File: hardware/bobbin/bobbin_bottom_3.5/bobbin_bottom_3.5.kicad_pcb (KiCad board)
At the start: 2 copper layers, 78.5 x 8.5 mm, 5 parts, among them J1 OC, J2 OC, J3 IC, J4 IC

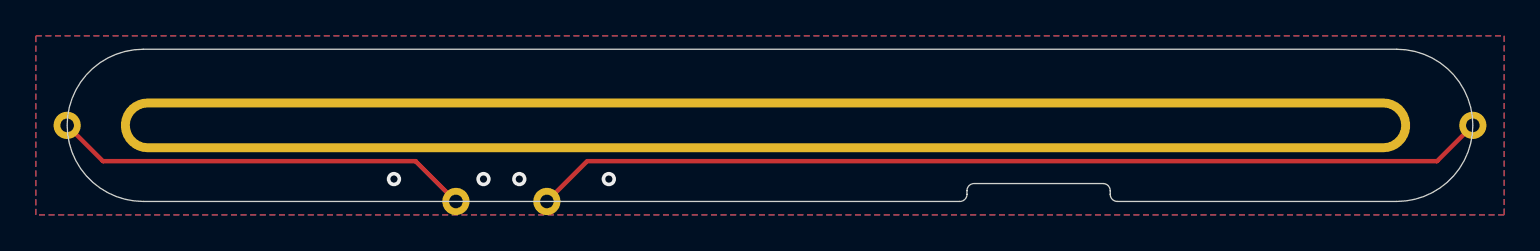
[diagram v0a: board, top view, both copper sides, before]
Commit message: adjusted for proper mouse-bites in panels
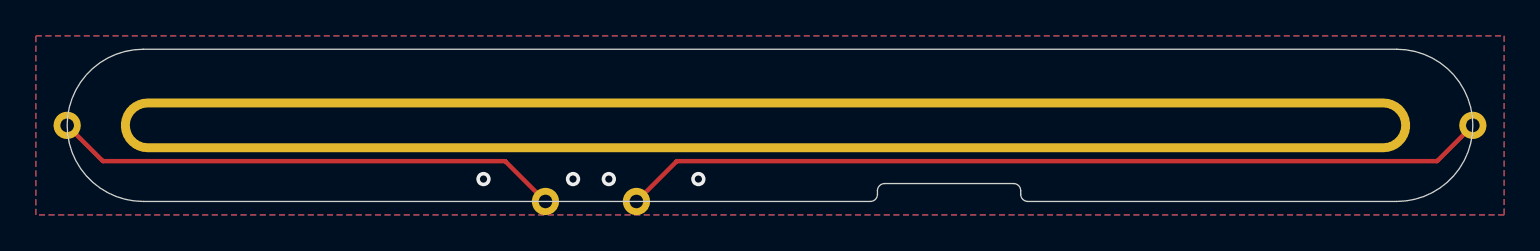
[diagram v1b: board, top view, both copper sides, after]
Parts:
- moved J1 5.00 mm to (122.5, 105.2)
- moved J4 5.00 mm to (117.5, 105.2)
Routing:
- net /OC: track 53.5 -> 48.5 mm
- net /IC: track 23.5 -> 28.5 mm
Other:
- outline, holes or cut-outs redrawn
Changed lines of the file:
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@@
   (net 3 "/IC")
   (footprint "cycfi_library:single-pad-1.52x1.52-th" (layer "F.Cu")
-    (at 117.54 105.25 180)
+    (at 122.54 105.25 180)
     (property "Sheetfile" "bobbin_bottom_3.5.kicad_sch")
     (property "Sheetname" "")
     (attr through_hole)
-    (fp_text reference "J1" (at 0 2.54 180) (layer "F.SilkS") hide
+    (fp_text reference "J1" (at 0 2.54) (layer "F.SilkS") hide
       (effects (font (size 1 1) (thickness 0.15)))
     )
-    (fp_text value "OC" (at 0 -2.54 180) (layer "F.Fab")
+    (fp_text value "OC" (at 0 -2.54) (layer "F.Fab")
       (effects (font (size 1 1) (thickness 0.15)))
     )
@@
   )
   (footprint "cycfi_library:single-pad-1.52x1.52-th" (layer "F.Cu")
-    (at 112.46 105.25)
+    (at 117.46 105.25)
     (property "Sheetfile" "bobbin_bottom_3.5.kicad_sch")
     (property "Sheetname" "")
@@
   (gr_line (start 95 100) (end 95 102) (layer "Dwgs.User") (width 0.01))
   (gr_arc (start 95 105.25) (mid 90.75 101) (end 95 96.75) (layer "Dwgs.User") (width 0.01))
-  (gr_line (start 140.6 105.25) (end 95 105.25) (layer "Dwgs.User") (width 0.01))
-  (gr_arc (start 116.778 105.25) (mid 117.54 104.488) (end 118.302 105.25) (layer "Dwgs.User") (width 0.01))
+  (gr_line (start 135.6 105.25) (end 95 105.25) (layer "Dwgs.User") (width 0.01))
+  (gr_arc (start 121.778 105.25) (mid 122.54 104.488) (end 123.302 105.25) (layer "Dwgs.User") (width 0.01))
   (gr_line (start 165 100) (end 165 102) (layer "Dwgs.User") (width 0.01))
-  (gr_arc (start 148.6 104.25) (mid 148.882843 104.367157) (end 149 104.65) (layer "Dwgs.User") (width 0.01))
-  (gr_arc (start 111.698 105.25) (mid 112.46 104.488) (end 113.222 105.25) (layer "Dwgs.User") (width 0.01))
-  (gr_arc (start 141 104.65) (mid 141.117157 104.367157) (end 141.4 104.25) (layer "Dwgs.User") (width 0.01))
+  (gr_arc (start 143.6 104.25) (mid 143.882843 104.367157) (end 144 104.65) (layer "Dwgs.User") (width 0.01))
+  (gr_arc (start 116.698 105.25) (mid 117.46 104.488) (end 118.222 105.25) (layer "Dwgs.User") (width 0.01))
+  (gr_arc (start 136 104.65) (mid 136.117157 104.367157) (end 136.4 104.25) (layer "Dwgs.User") (width 0.01))
   (gr_arc (start 90.818311 100.241068) (mid 91.512 101) (end 90.818311 101.758932) (layer "Dwgs.User") (width 0.01))
-  (gr_line (start 141.4 104.25) (end 148.6 104.25) (layer "Dwgs.User") (width 0.01))
+  (gr_line (start 136.4 104.25) (end 143.6 104.25) (layer "Dwgs.User") (width 0.01))
   (gr_line (start 95 96.75) (end 165 96.75) (layer "Dwgs.User") (width 0.01))
-  (gr_line (start 141 104.85) (end 141 104.65) (layer "Dwgs.User") (width 0.01))
+  (gr_line (start 136 104.85) (end 136 104.65) (layer "Dwgs.User") (width 0.01))
   (gr_arc (start 169.181689 101.758932) (mid 168.488 101) (end 169.181689 100.241068) (layer "Dwgs.User") (width 0.01))
-  (gr_line (start 165 105.25) (end 149.4 105.25) (layer "Dwgs.User") (width 0.01))
+  (gr_line (start 165 105.25) (end 144.4 105.25) (layer "Dwgs.User") (width 0.01))
   (gr_line (start 95 100) (end 165 100) (layer "Dwgs.User") (width 0.01))
-  (gr_arc (start 149.4 105.25) (mid 149.117157 105.132843) (end 149 104.85) (layer "Dwgs.User") (width 0.01))
-  (gr_line (start 149 104.65) (end 149 104.85) (layer "Dwgs.User") (width 0.01))
+  (gr_arc (start 144.4 105.25) (mid 144.117157 105.132843) (end 144 104.85) (layer "Dwgs.User") (width 0.01))
+  (gr_line (start 144 104.65) (end 144 104.85) (layer "Dwgs.User") (width 0.01))
   (gr_line (start 95 102) (end 165 102) (layer "Dwgs.User") (width 0.01))
-  (gr_arc (start 141 104.85) (mid 140.882843 105.132843) (end 140.6 105.25) (layer "Dwgs.User") (width 0.01))
+  (gr_arc (start 136 104.85) (mid 135.882843 105.132843) (end 135.6 105.25) (layer "Dwgs.User") (width 0.01))
   (gr_arc (start 165 96.75) (mid 169.25 101) (end 165 105.25) (layer "Edge.Cuts") (width 0.01))
-  (gr_arc (start 141 104.85) (mid 140.882843 105.132843) (end 140.6 105.25) (layer "Edge.Cuts") (width 0.01))
-  (gr_line (start 165 105.25) (end 149.4 105.25) (layer "Edge.Cuts") (width 0.01))
+  (gr_arc (start 136 104.85) (mid 135.882843 105.132843) (end 135.6 105.25) (layer "Edge.Cuts") (width 0.01))
+  (gr_line (start 165 105.25) (end 144.4 105.25) (layer "Edge.Cuts") (width 0.01))
   (gr_arc (start 95 105.25) (mid 90.75 101) (end 95 96.75) (layer "Edge.Cuts") (width 0.01))
   (gr_line (start 95 96.75) (end 165 96.75) (layer "Edge.Cuts") (width 0.01))
-  (gr_arc (start 148.6 104.25) (mid 148.882843 104.367157) (end 149 104.65) (layer "Edge.Cuts") (width 0.01))
-  (gr_arc (start 149.4 105.25) (mid 149.117157 105.132843) (end 149 104.85) (layer "Edge.Cuts") (width 0.01))
-  (gr_line (start 149 104.65) (end 149 104.85) (layer "Edge.Cuts") (width 0.01))
-  (gr_line (start 141 104.85) (end 141 104.65) (layer "Edge.Cuts") (width 0.01))
-  (gr_line (start 141.4 104.25) (end 148.6 104.25) (layer "Edge.Cuts") (width 0.01))
-  (gr_arc (start 141 104.65) (mid 141.117157 104.367157) (end 141.4 104.25) (layer "Edge.Cuts") (width 0.01))
-  (gr_line (start 140.6 105.25) (end 95 105.25) (layer "Edge.Cuts") (width 0.01))
-  (via (at 109 104) (size 0.8) (drill 0.4) (layers "F.Cu" "B.Cu") (free) (net 1))
+  (gr_arc (start 143.6 104.25) (mid 143.882843 104.367157) (end 144 104.65) (layer "Edge.Cuts") (width 0.01))
+  (gr_arc (start 144.4 105.25) (mid 144.117157 105.132843) (end 144 104.85) (layer "Edge.Cuts") (width 0.01))
+  (gr_line (start 144 104.65) (end 144 104.85) (layer "Edge.Cuts") (width 0.01))
+  (gr_line (start 136 104.85) (end 136 104.65) (layer "Edge.Cuts") (width 0.01))
+  (gr_line (start 136.4 104.25) (end 143.6 104.25) (layer "Edge.Cuts") (width 0.01))
+  (gr_arc (start 136 104.65) (mid 136.117157 104.367157) (end 136.4 104.25) (layer "Edge.Cuts") (width 0.01))
+  (gr_line (start 135.6 105.25) (end 95 105.25) (layer "Edge.Cuts") (width 0.01))
   (via (at 114 104) (size 0.8) (drill 0.4) (layers "F.Cu" "B.Cu") (free) (net 1))
-  (via (at 116 104) (size 0.8) (drill 0.4) (layers "F.Cu" "B.Cu") (free) (net 1))
+  (via (at 119 104) (size 0.8) (drill 0.4) (layers "F.Cu" "B.Cu") (free) (net 1))
   (via (at 121 104) (size 0.8) (drill 0.4) (layers "F.Cu" "B.Cu") (free) (net 1))
-  (segment (start 117.54 105.25) (end 119.79 103) (width 0.25) (layer "F.Cu") (net 2))
-  (segment (start 119.79 103) (end 167.25 103) (width 0.25) (layer "F.Cu") (net 2))
+  (via (at 126 104) (size 0.8) (drill 0.4) (layers "F.Cu" "B.Cu") (free) (net 1))
+  (segment (start 122.54 105.25) (end 124.79 103) (width 0.25) (layer "F.Cu") (net 2))
+  (segment (start 124.79 103) (end 167.25 103) (width 0.25) (layer "F.Cu") (net 2))
   (segment (start 167.25 103) (end 169.25 101) (width 0.25) (layer "F.Cu") (net 2))
-  (segment (start 110.21 103) (end 92.75 103) (width 0.25) (layer "F.Cu") (net 3))
-  (segment (start 112.46 105.25) (end 110.21 103) (width 0.25) (layer "F.Cu") (net 3))
+  (segment (start 115.21 103) (end 92.75 103) (width 0.25) (layer "F.Cu") (net 3))
+  (segment (start 117.46 105.25) (end 115.21 103) (width 0.25) (layer "F.Cu") (net 3))
   (segment (start 92.75 103) (end 90.75 101) (width 0.25) (layer "F.Cu") (net 3))
   (zone (net 1) (net_name "GND") (layer "F.Cu") (hatch edge 0.508)
